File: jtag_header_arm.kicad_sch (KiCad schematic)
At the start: 6 parts, among them J5 02x10_2.54mm_Header_Odd_Even

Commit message: updates JTAG header naming etc. Refs: #1
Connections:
- net SWCLK/TCLK renamed SWCLK_TCLK
- net SWDIO/TMS renamed SWDIO_TMS
- net SWO/TDO renamed SWO_TDO
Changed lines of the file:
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@@
 		)
 	)
-	(hierarchical_label "SWO{slash}TDO"
+	(hierarchical_label "SWO_TDO"
 		(shape bidirectional)
 		(at 124.46 78.74 180)
@@
 		)
 	)
-	(hierarchical_label "SWCLK{slash}TCLK"
+	(hierarchical_label "SWCLK_TCLK"
 		(shape bidirectional)
 		(at 124.46 73.66 180)
@@
 		)
 	)
-	(hierarchical_label "SWDIO{slash}TMS"
+	(hierarchical_label "SWDIO_TMS"
 		(shape bidirectional)
 		(at 124.46 71.12 180)

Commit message: updates component details for ordering. Refs: #1
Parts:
- J5: Digikey (none) -> 2057-BHR-20-VUA-ND; LCSC (none) -> C598987; Mouser (none) -> 737-BHR-20-VUA
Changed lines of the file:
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@@
+			)
+		)
+		(property "Dielectric" ""
+			(at 104.14 90.17 0)
+			(effects
+				(font
+					(size 1.27 1.27)
+				)
+				(hide yes)
+			)
+		)
+		(property "Dielectric_type" ""
+			(at 104.14 90.17 0)
+			(effects
+				(font
+					(size 1.27 1.27)
+				)
+				(hide yes)
+			)
+		)
+		(property "LSCS" ""
+			(at 104.14 90.17 0)
+			(effects
+				(font
+					(size 1.27 1.27)
+				)
+				(hide yes)
+			)
+		)
+		(property "Max Current" ""
+			(at 104.14 90.17 0)
+			(effects
+				(font
+					(size 1.27 1.27)
+				)
+				(hide yes)
 			)
 		)
@@
 			)
 		)
+		(property "Dielectric" ""
+			(at 93.98 90.17 0)
+			(effects
+				(font
+					(size 1.27 1.27)
+				)
+				(hide yes)
+			)
+		)
+		(property "Dielectric_type" ""
+			(at 93.98 90.17 0)
+			(effects
+				(font
+					(size 1.27 1.27)
+				)
+				(hide yes)
+			)
+		)
+		(property "LSCS" ""
+			(at 93.98 90.17 0)
+			(effects
+				(font
+					(size 1.27 1.27)
+				)
+				(hide yes)
+			)
+		)
+		(property "Max Current" ""
+			(at 93.98 90.17 0)
+			(effects
+				(font
+					(size 1.27 1.27)
+				)
+				(hide yes)
+			)
+		)
 		(pin "1"
 		)
@@
 			)
 		)
+		(property "Dielectric" ""
+			(at 127 57.15 0)
+			(effects
+				(font
+					(size 1.27 1.27)
+				)
+				(hide yes)
+			)
+		)
+		(property "Dielectric_type" ""
+			(at 127 57.15 0)
+			(effects
+				(font
+					(size 1.27 1.27)
+				)
+				(hide yes)
+			)
+		)
+		(property "LSCS" ""
+			(at 127 57.15 0)
+			(effects
+				(font
+					(size 1.27 1.27)
+				)
+				(hide yes)
+			)
+		)
+		(property "Max Current" ""
+			(at 127 57.15 0)
+			(effects
+				(font
+					(size 1.27 1.27)
+				)
+				(hide yes)
+			)
+		)
 		(pin "1"
 		)
@@
 			)
 		)
+		(property "Dielectric" ""
+			(at 114.3 90.17 0)
+			(effects
+				(font
+					(size 1.27 1.27)
+				)
+				(hide yes)
+			)
+		)
+		(property "Dielectric_type" ""
+			(at 114.3 90.17 0)
+			(effects
+				(font
+					(size 1.27 1.27)
+				)
+				(hide yes)
+			)
+		)
+		(property "LSCS" ""
+			(at 114.3 90.17 0)
+			(effects
+				(font
+					(size 1.27 1.27)
+				)
+				(hide yes)
+			)
+		)
+		(property "Max Current" ""
+			(at 114.3 90.17 0)
+			(effects
+				(font
+					(size 1.27 1.27)
+				)
+				(hide yes)
+			)
+		)
 		(pin "1"
 		)
@@
 			)
 		)
+		(property "Manufacturer_No" ""
+			(at 132.08 73.66 0)
+			(effects
+				(font
+					(size 1.27 1.27)
+				)
+				(hide yes)
+			)
+		)
+		(property "Mouser" "737-BHR-20-VUA"
+			(at 132.08 73.66 0)
+			(effects
+				(font
+					(size 1.27 1.27)
+				)
+				(hide yes)
+			)
+		)
+		(property "Digikey" "2057-BHR-20-VUA-ND"
+			(at 132.08 73.66 0)
+			(effects
+				(font
+					(size 1.27 1.27)
+				)
+				(hide yes)
+			)
+		)
+		(property "LCSC" "C598987"
+			(at 132.08 73.66 0)
+			(effects
+				(font
+					(size 1.27 1.27)
+				)
+				(hide yes)
+			)
+		)
 		(pin "1"
 		)
@@
 			(at 139.7 57.15 0)
 			(effects
+				(font
+					(size 1.27 1.27)
+				)
+				(hide yes)
+			)
+		)
+		(property "Dielectric" ""
+			(at 139.7 57.15 0)
+			(effects
+				(font
+					(size 1.27 1.27)
+				)
+				(hide yes)
+			)
+		)
+		(property "Dielectric_type" ""
+			(at 139.7 57.15 0)
+			(effects
+				(font
+					(size 1.27 1.27)
+				)
+				(hide yes)
+			)
+		)
+		(property "LSCS" ""
+			(at 139.7 57.15 0)
+			(effects
+				(font
+					(size 1.27 1.27)
+				)
+				(hide yes)
+			)
+		)
+		(property "Max Current" ""
+			(at 139.7 57.15 0)
+			(effects

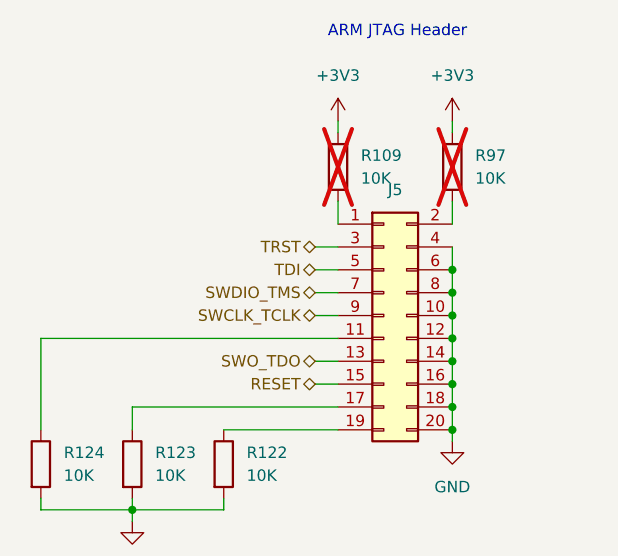
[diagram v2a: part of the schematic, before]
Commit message: 1: ading 0R on the JTAG TRST
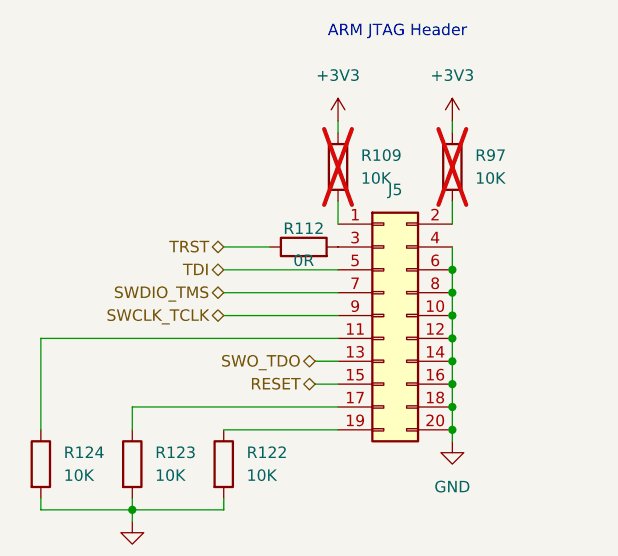
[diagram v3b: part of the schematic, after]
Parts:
- added R112: 0R, KL_Footprints:R_2512, symbol KL_R:R_0R_2W_5_2512
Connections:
- net TRST: now also R112.1; no longer J5.3 (Pin_3)
- new net: J5.3 (Pin_3), R112.2
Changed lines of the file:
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@@
+	(wire
+		(pts
+			(xy 114.3 66.04) (xy 119.38 66.04)
+		)
+		(stroke
+			(width 0)
+			(type default)
+		)
+	)
 	(wire
 		(pts
@@
 	(wire
 		(pts
-			(xy 124.46 68.58) (xy 127 68.58)
+			(xy 114.3 68.58) (xy 127 68.58)
 		)
 		(stroke
@@
 	(wire
 		(pts
-			(xy 124.46 73.66) (xy 127 73.66)
-		)
-		(stroke
-			(width 0)
-			(type default)
-		)
-	)
-	(wire
-		(pts
-			(xy 127 66.04) (xy 124.46 66.04)
+			(xy 114.3 73.66) (xy 127 73.66)
 		)
 		(stroke
@@
 	(wire
 		(pts
-			(xy 124.46 71.12) (xy 127 71.12)
+			(xy 114.3 71.12) (xy 127 71.12)
 		)
 		(stroke
@@
 	(hierarchical_label "SWCLK_TCLK"
 		(shape bidirectional)
-		(at 124.46 73.66 180)
+		(at 114.3 73.66 180)
 		(effects
 			(font
@@
 	(hierarchical_label "TDI"
 		(shape bidirectional)
-		(at 124.46 68.58 180)
+		(at 114.3 68.58 180)
 		(effects
 			(font
@@
 	(hierarchical_label "SWDIO_TMS"
 		(shape bidirectional)
-		(at 124.46 71.12 180)
+		(at 114.3 71.12 180)
 		(effects
 			(font
@@
 	(hierarchical_label "TRST"
 		(shape bidirectional)
-		(at 124.46 66.04 180)
+		(at 114.3 66.04 180)
 		(effects
 			(font
@@
 		)
 	)
+	(symbol
+		(lib_id "KL_R:R_0R_2W_5_2512")
+		(at 123.19 66.04 90)
+		(unit 1)
+		(exclude_from_sim no)
+		(in_bom yes)
+		(on_board yes)
+		(dnp no)
+		(property "Reference" "R112"
+			(at 123.19 64.008 90)
+			(effects
+				(font
+					(size 1.27 1.27)
+				)
+			)
+		)
+		(property "Value" "0R"
+			(at 123.19 67.564 90)
+			(effects
+				(font
+					(size 1.27 1.27)
+				)
+			)
+		)
+		(property "Footprint" "KL_Footprints:R_2512"
+			(at 123.19 67.818 90)
+			(effects
+				(font
+					(size 1.27 1.27)
+				)
+				(hide yes)
+			)
+		)
+		(property "Datasheet" "~"
+			(at 123.19 66.04 0)
+			(effects
+				(font
+					(size 1.27 1.27)
+				)
+				(hide yes)
+			)
+		)
+		(property "Description" "Resistor"
+			(at 123.19 66.04 0)
+			(effects
+				(font
+					(size 1.27 1.27)
+				)
+				(hide yes)
+			)
+		)
+		(property "Power" "2"
+			(at 123.19 66.04 0)
+			(effects
+				(font
+					(size 1.27 1.27)
+				)
+				(hide yes)
+			)
+		)
+		(property "Tolerance" "5"
+			(at 123.19 66.04 0)
+			(effects
+				(font
+					(size 1.27 1.27)
+				)
+				(hide yes)
+			)
+		)
+		(property "Mouser" "652-CRF2512-J-000ELF "
+			(at 123.19 66.04 0)
+			(effects
+				(font
+					(size 1.27 1.27)
+				)
+				(hide yes)
+			)
+		)
+		(property "Digikey" "118-CRF2512-J/-000ELFCT-ND"
+			(at 123.19 66.04 0)
+			(effects
+				(font
+					(size 1.27 1.27)
+				)
+				(hide yes)
+			)
+		)
+		(property "LCSC" "C2778666"
+			(at 123.19 66.04 0)
+			(effects
+				(font
+					(size 1.27 1.27)
+				)
+				(hide yes)
+			)
+		)
+		(property "Farnell" ""
+			(at 123.19 66.04 0)
+			(effects
+				(font
+					(size 1.27 1.27)
+				)
+				(hide yes)
+			)
+		)
+		(property "Package (in)" "2512"
+			(at 123.19 66.04 0)
+			(effects
+				(font
+					(size 1.27 1.27)
+				)
+				(hide yes)
+			)
+		)
+		(property "Dielectric" ""
+			(at 123.19 66.04 90)
+			(effects
+				(font
+					(size 1.27 1.27)
+				)
+				(hide yes)
+			)
+		)
+		(property "Dielectric_type" ""
+			(at 123.19 66.04 90)
+			(effects
+				(font
+					(size 1.27 1.27)
+				)
+				(hide yes)
+			)
+		)
+		(property "LSCS" ""
+			(at 123.19 66.04 90)
+			(effects
+				(font
+					(size 1.27 1.27)
+				)
+				(hide yes)
+			)
+		)
+		(property "Max Current" ""
+			(at 123.19 66.04 90)
+			(effects
+				(font
+					(size 1.27 1.27)
+				)
+				(hide yes)
+			)
+		)
+		(pin "2"
+		)
+		(pin "1"
+		)
+		(instances
+			(project "shish-lan"
+				(path "/d4536448-b109-4159-96e2-3dc21baf2d6e/06488c82-a47f-4277-b0ee-3bd211d8922a/54dd0313-e11b-4c5a-bb43-942dea0cd180"
+					(reference "R112")
+					(unit 1)
+				)
+			)
+		)
+	)
